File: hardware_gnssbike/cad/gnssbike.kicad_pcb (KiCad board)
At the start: 4 copper layers, 34 x 90 mm, 145 parts, among them J101 HRO TYPE-C-31-M-12, J102 JST SM06B-GHS-TB, J103 JST S4B-ZR-SM4A-TF, J201 Tag-Connect TC2030-NL, J302 Hirose U.FL-R-SMT-1, J401 Hirose FH12-10S-0.5SH(55), J402 Molex 503480-0500, Q401 DMG1012T-7, Q601 DMG1012T-7, Q602 DMG1012T-7, Q603 DMG1012T-7, SW601 XunPu TS-1088R-02026, SW602 XunPu TS-1088R-02026, SW603 XunPu TS-1088R-02026, U101 nPM1300-QEAA, U102 MAX17262REWL, U103 ADP5091ACPZ-2, U104 TPS7A0218PDQN, U201 MinewSemi ME54BS13, U301 u-blox MAX-F10S, U302 TI TXU0204BQAR, U501 MX25R6435F, U502 Bosch BMP585, U503 Bosch BMI270, U504 Memsic MMC5603NJ, U505 TI OPT3001DNPR

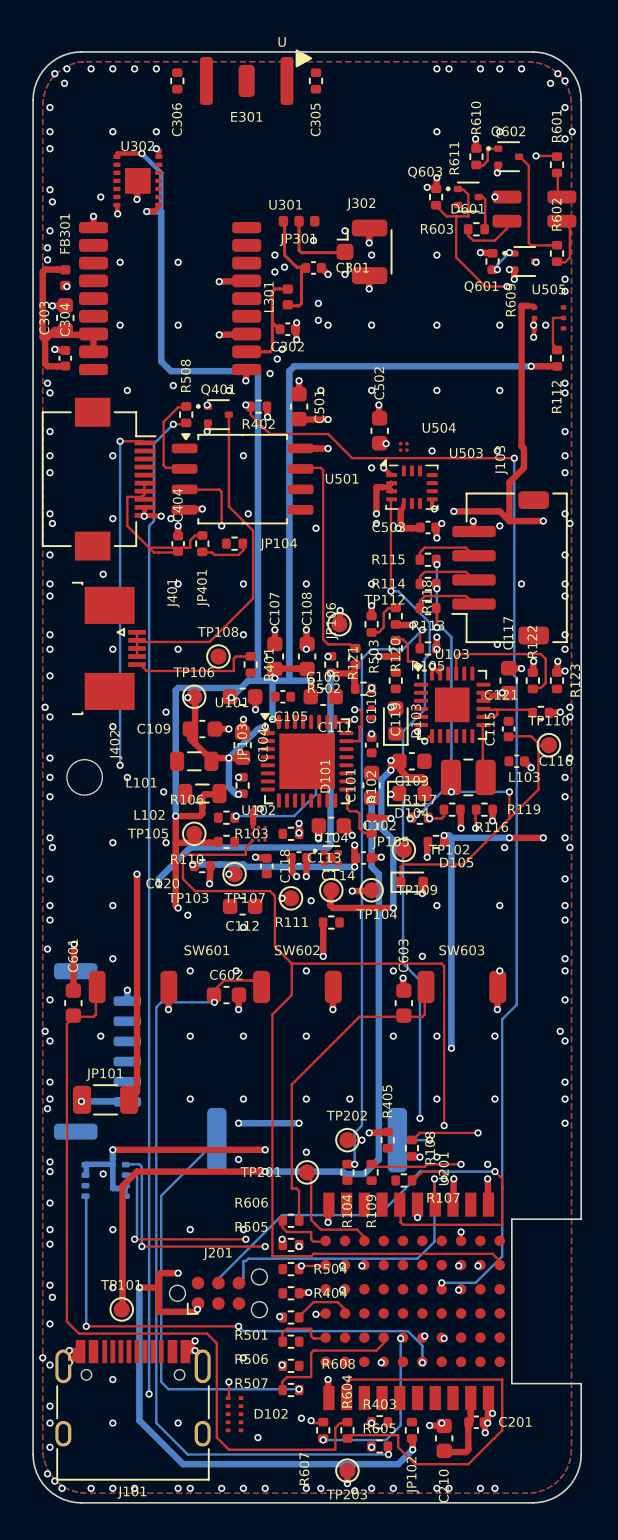
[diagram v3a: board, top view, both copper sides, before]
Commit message: feat(hardware): real symbols and real 3D models, from KiCad's own libraries
Two of the owner's asks in one commit, because they turned out to be the
same idea: stop drawing what already exists, reviewed, in the library.

THE SCHEMATIC. 36 of the parts were rectangles with pins around them - the
ICs, the connectors and the display - and a rectangle says nothing. Anyone
reading a schematic recognises a coaxial connector by the circle with the
dot, a switch by the contact that opens, a MOSFET by the channel and the
arrow.

ksym.py reads a symbol out of KiCad's own library - 21.110 of them, every
one reviewed against the KLC - and embeds it in our schematic with our
properties. simbolos.py says which part uses which. Eleven are in, and
ksym.checar() verifies every one pin number by pin number, because a
pretty symbol with the wire on the wrong pin is worse than a correct
rectangle. RF_GPS:MAX-M10S is literally our receiver: 18 pins, 18 names,
the same LCC-18.

Three symbols verify clean and still break the drawing, and they are
parked with the reason MEASURED rather than "did not work": the ADP5091
puts MPPT on the bottom edge beside its three ground pins and the ground
power symbol lands on the MPPT wire; the USB-C stacks four contacts per
point with 5,08 mm stubs and VBUS meets CC1; the ten pins of the display
FPC are all on one edge and two wires cannot reach. Each needs work
somewhere else - the power symbol placer, the placement - not a different
symbol.

Three bugs were found and fixed on the way, all in the router, all of the
same family: it assumed things about symbols that are only true of the
ones this project draws.

  - Symbols from KiCad are NOT centred on their origin. A
    Conn_01x10_Socket has its drawing at x -1,27 to 0 and all ten pins at
    x = -5,08. Treated as centred, pins fall inside the obstacle, the
    router cannot reach them from outside and goes over them instead -
    and two nets that touch are one net, with nothing in the drawing
    sa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
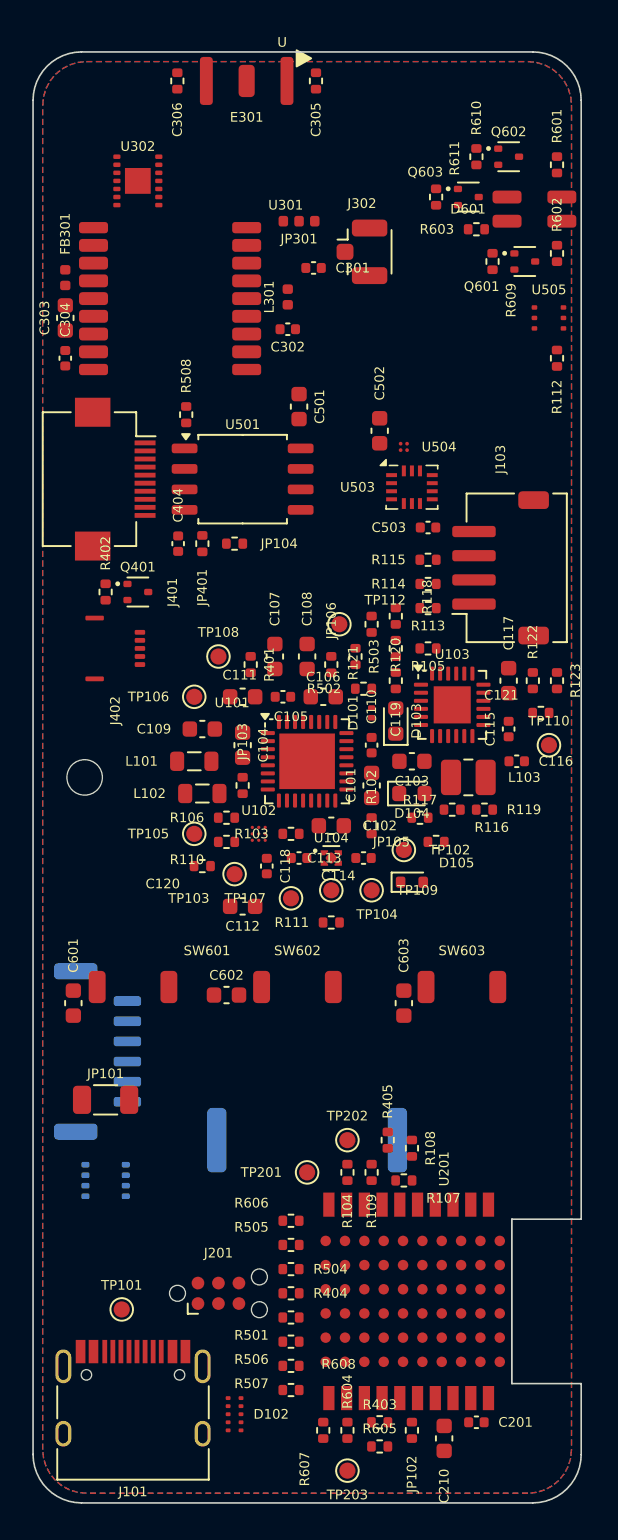
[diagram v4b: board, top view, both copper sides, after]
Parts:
- J402: value Molex 503480-0500 -> HCTL HC-FPC-05-10-5RLTAG; footprint Connector_FFC-FPC:TE_0-1734839-5_1x05-1MP_P0.5mm_Horizontal -> gnssbike:HC-FPC-05-10-5RLTAG
- U103: footprint Package_DFN_QFN:QFN-24-1EP_4x4mm_P0.5mm_EP2.15x2.15mm -> Package_CSP:LFCSP-24-1EP_4x4mm_P0.5mm_EP2.3x2.3mm
- moved R402 14.9 mm to (29.5, 58.5), turned to 90 degrees
- moved Q401 12.1 mm to (31.5, 58.5)
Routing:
- net 3V0: track 217.3 -> 0.00 mm, vias 18 -> 0
- net 3V0_SENS: track 116.6 -> 0.00 mm, vias 13 -> 0
- net DISP_SCK: track 89.0 -> 0.00 mm, vias 3 -> 0
- net RGB_B: track 80.6 -> 0.00 mm, vias 2 -> 0
- net VSYS: track 78.7 -> 0.00 mm, vias 5 -> 0
- net NOR_MISO: track 76.8 -> 0.00 mm, vias 3 -> 0
- net PWR_SDA: track 75.8 -> 0.00 mm, vias 2 -> 0
- net BL_PWM: track 75.6 -> 0.00 mm, vias 4 -> 0
- net SD3V0: track 69.4 -> 0.00 mm, vias 4 -> 0
- net GND: track 66.3 -> 0.00 mm, vias 310 -> 0
- net CC1: track 62.8 -> 0.00 mm, vias 2 -> 0
- net IMU_INT: track 57.6 -> 0.00 mm, vias 3 -> 0
- net VBAT_SYS: track 54.5 -> 0.00 mm, vias 7 -> 0
- net 1V8: track 49.7 -> 0.00 mm, vias 5 -> 0
- net KEY_C_SW: track 49.2 -> 0.00 mm, vias 2 -> 0
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
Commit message: fix(hardware): the debug connector had RESET on the wrong contact
This one would have cost a board. The Tag-Connect TC2030 footprint had
pin 3 as no-connect and RESET on pin 6. The manufacturer's own data
sheet, TC2030-CTX_1.pdf, table "Connections", says the opposite: on the
six-pin footprint it is 3 = nRESET and 6 = SWO/TDO.

Where the mistake came from is worth writing down, because it is easy to
make twice: 1 VCC, 2 SWDIO, 3 GND, 4 SWCLK, 5 GND, 6 SWO is the
numbering of the ten-way Cortex header on the PROBE side, not of the
six-pin footprint on the board. Mixing the two gives exactly what was
written here.

What it would have done: the probe's nRESET is an open drain output, so
it would have driven nothing, and the MCU's reset would have hung off
the probe's SWO INPUT. Nothing burns - SWO runs target to probe, there
is no short - but the debugger can never reset the target: no connect
under reset, no pin reset. On an nRF54LM20A that reboots from task_wdt
or reconfigures its SWD pins, that removes the standard way out and
leaves only a full CTRL-AP erase.

The documentation carried a worse version still. 06 had GND on contact 3,
which fabricated would tie the probe's open-drain nRESET to copper
ground and hold the target in reset forever.

The project's own notes had predicted this exact variant - 06 carried a
CAUTION saying so and README an open checklist item. It was that one, and
it was caught before layout. Both are now closed, and the connector's
pin 6 is recorded as SWO with what is still unknown about it: which pad
of the ME54BS13 exposes SWO, which would give printf over ITM during
bring-up.

Fixed in parts.py, nets.py, 03-netlist.md, 06-conectores-e-pontos-de-teste.md,
07-sequencias-e-protecao.md and README.md.

Verified: check_sch and check_pcb pass, 78 of 78 diagrams render, 1529
links and none broken.
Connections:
- J201 pad 3: (no net) -> MOD_RESET
- J201 pad 6: MOD_RESET -> (no net)
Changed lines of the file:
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@@
 	)
 	(pad "3" connect circle
+		(net 57 "MOD_RESET")
 		(at 0 0.635)
 		(size 0.7874 0.7874)
@@
 	)
 	(pad "6" connect circle
-		(net 57 "MOD_RESET")
 		(at 1.27 -0.635)
 		(size 0.7874 0.7874)
